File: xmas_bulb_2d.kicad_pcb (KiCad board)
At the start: 2 copper layers, 61.8 x 66.5 mm, 30 parts, among them SW1 SW_DPDT_x2, U1 ATtiny13A-SSU

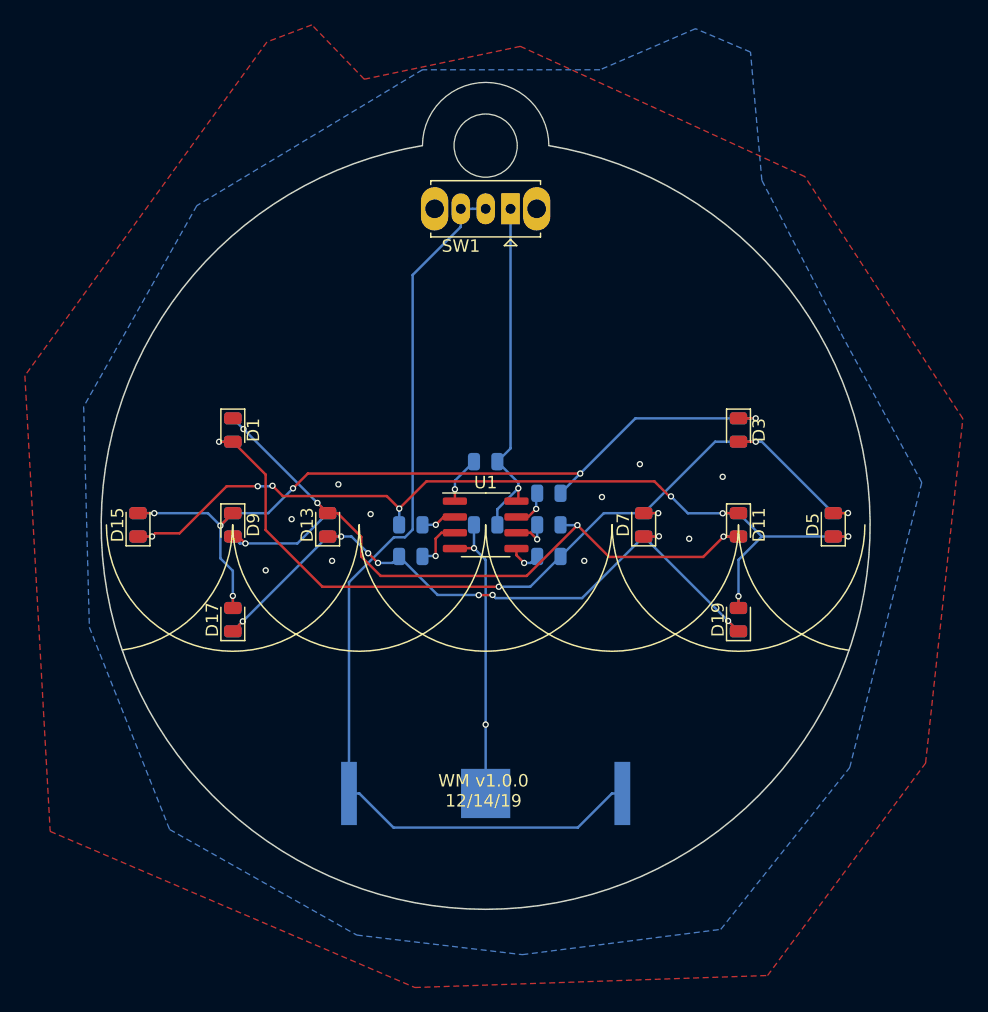
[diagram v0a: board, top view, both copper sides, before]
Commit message: Actually connect D1
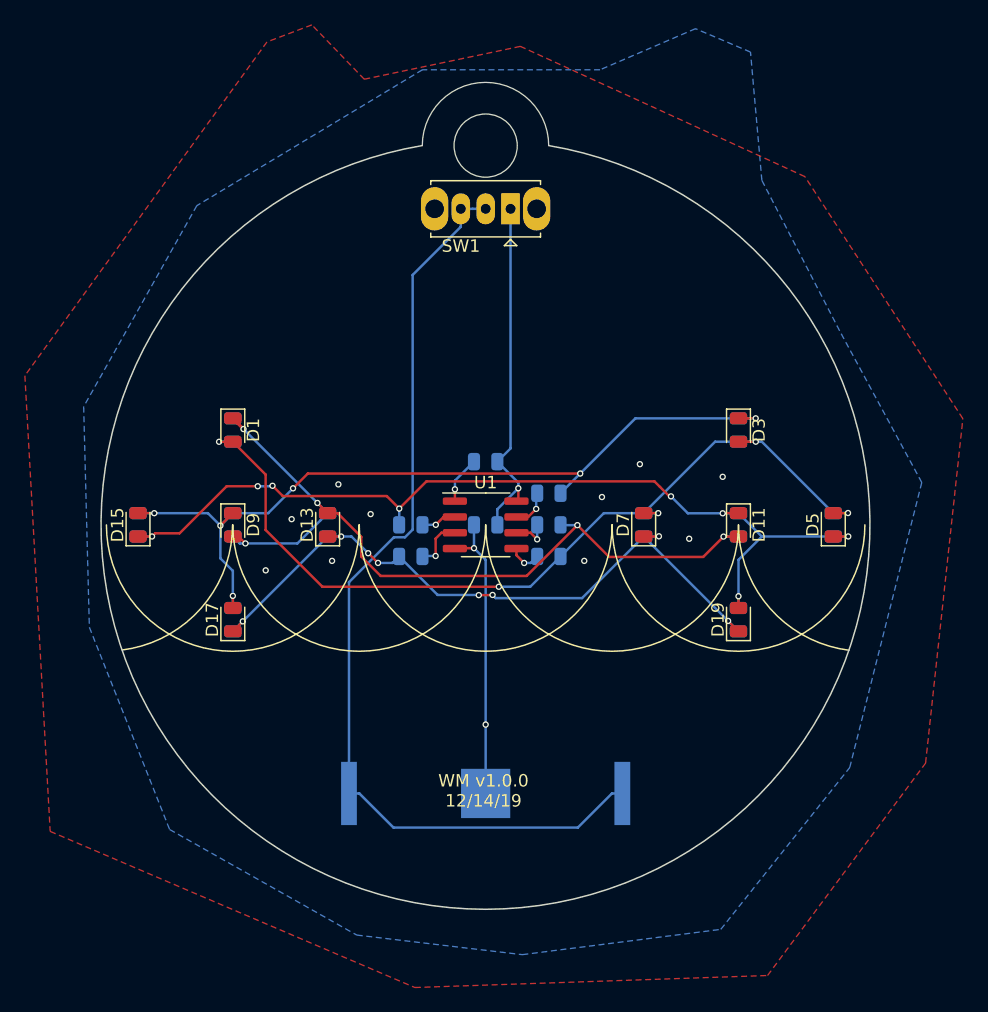
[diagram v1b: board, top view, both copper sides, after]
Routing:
- net Net-(D1-Pad1): track 64.1 -> 65.3 mm
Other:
- outline, holes or cut-outs redrawn
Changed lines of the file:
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@@
-(kicad_pcb (version 20171130) (host pcbnew "(5.1.4)-1")
+(kicad_pcb (version 20171130) (host pcbnew "(5.1.2)-1")
   (general
     (thickness 1.6)
     (drawings 23)
-    (tracks 245)
+    (tracks 246)
     (zones 0)
     (modules 30)
@@
   )
   (setup
-    (last_trace_width 0.2)
+    (last_trace_width 0.25)
     (user_trace_width 0.2)
     (trace_clearance 0.2)
@@
   (gr_arc (start 132.08 60.96) (end 121.92 60.96) (angle -180) (layer F.SilkS) (width 0.12))
   (gr_line (start 152.4 27.94) (end 152.4 99.06) (layer Cmts.User) (width 0.15))
-  (gr_arc (start 152.4 60.96) (end 147.320001 30.480001) (angle -341.0707116) (layer Edge.Cuts) (width 0.12))
+  (gr_arc (start 152.386889 60.957818) (end 147.30689 30.477819) (angle -341.075355) (layer Edge.Cuts) (width 0.12))
   (gr_text "WM v1.0.0\n12/14/19" (at 152.2222 82.3341) (layer F.SilkS)
     (effects (font (size 1 1) (thickness 0.15)))
@@
   (gr_line (start 152.4 104.14) (end 114.3 104.14) (layer Cmts.User) (width 0.15))
   (gr_line (start 152.4 104.14) (end 190.5 104.14) (layer Cmts.User) (width 0.15))
-  (gr_circle (center 152.4 30.48) (end 152.4 27.94) (layer Edge.Cuts) (width 0.05))
-  (gr_arc (start 152.4 30.48) (end 157.48 30.48) (angle -180) (layer Edge.Cuts) (width 0.05))
+  (gr_circle (center 152.4 30.48) (end 154.94 30.48) (layer Edge.Cuts) (width 0.05))
+  (gr_arc (start 152.38689 30.477819) (end 157.46689 30.477819) (angle -180) (layer Edge.Cuts) (width 0.05))
   (segment (start 162.55 82.55) (end 163.385 82.55) (width 0.2) (layer B.Cu) (net 1))
   (segment (start 159.81 85.29) (end 162.55 82.55) (width 0.2) (layer B.Cu) (net 1))
@@
   (segment (start 155.69184 65.06718) (end 159.77362 60.9854) (width 0.2) (layer F.Cu) (net 5))
   (segment (start 143.963678 65.06718) (end 155.69184 65.06718) (width 0.2) (layer F.Cu) (net 5))
+  (segment (start 132.08 52.4025) (end 132.9361 53.2586) (width 0.25) (layer F.Cu) (net 5))
   (segment (start 174.595 61.8975) (end 172.72 60.0225) (width 0.2) (layer B.Cu) (net 6))
   (segment (start 180.34 61.8975) (end 174.595 61.8975) (width 0.2) (layer B.Cu) (net 6))
